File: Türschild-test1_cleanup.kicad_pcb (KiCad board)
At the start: 2 copper layers, 90.2 x 76.2 mm, 84 parts, among them J1 Conn_01x03_Male, J3 USB_B_Micro, J4 Conn_01x24_MountingPin, Q3 Si1442DH, U1 BQ25570, U2 BQ27441-G1, U3 ESP32-WROOM-32, U4 CP2102N-A01-GQFN28

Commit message: HowTo Changes mit Daniel
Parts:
- removed Q3: Si1442DH, Package_TO_SOT_SMD:SOT-363_SC-70-6
- added BT1: 3,7V, Battery:BatteryHolder_Bulgin_BX0036_1xC, F.Cu at (201.7, 34.9)
- added C12: 1µ, Capacitor_SMD:C_0603_1608Metric_Pad1.05x0.95mm_HandSolder, F.Cu at (277.0, 22.8)
- added C24: 100n, Capacitor_SMD:C_0603_1608Metric_Pad1.05x0.95mm_HandSolder, F.Cu at (266.2, 31.9)
- added C25: 100n, Capacitor_SMD:C_0603_1608Metric_Pad1.05x0.95mm_HandSolder, F.Cu at (247.8, 53.2)
- added C26: 4u7, Capacitor_SMD:C_0805_2012Metric_Pad1.15x1.40mm_HandSolder, F.Cu at (240.9, 55.3)
- added J2: Conn_01x03_Female, Connector_PinSocket_2.00mm:PinSocket_1x03_P2.00mm_Vertical_SMD_Pin1Right, F.Cu at (224.9, 56.2)
- added Q1: IRLML2502PbF, Package_TO_SOT_SMD:SOT-23, F.Cu at (261.4, 35.8)
- added R21: 0R, Resistor_SMD:R_0603_1608Metric_Pad1.05x0.95mm_HandSolder, F.Cu at (244.9, 60.7)
- added R22: 1K, Resistor_SMD:R_0603_1608Metric_Pad1.05x0.95mm_HandSolder, F.Cu at (264.7, 40.8)
- added R23: 4K7, Resistor_SMD:R_0603_1608Metric_Pad1.05x0.95mm_HandSolder, F.Cu at (123.2, 121.0)
- added SC1: Solar_Cells, Connector_PinHeader_2.54mm:PinHeader_1x02_P2.54mm_Horizontal, F.Cu at (201.2, 54.2)
- added U5: LM1117-3.3, Package_TO_SOT_SMD:SOT-223-3_TabPin2, F.Cu at (264.1, 25.5)
- added U6: WE-TVS-82400152, Package_TO_SOT_SMD:SOT-563, F.Cu at (119.8, 115.7)
- C1, C10, C11, C2: footprint Capacitor_SMD:C_0603_1608Metric -> Capacitor_SMD:C_0805_2012Metric_Pad1.15x1.40mm_HandSolder
- C13, C14, C15, C16, C17, C18, C19, C20, C21, C22, C5, C6, C7, C8, C9: footprint Capacitor_SMD:C_0603_1608Metric -> Capacitor_SMD:C_0603_1608Metric_Pad1.05x0.95mm_HandSolder
- C3, C4: value 0,1µF -> 100n; footprint Capacitor_SMD:C_0603_1608Metric -> Capacitor_SMD:C_0603_1608Metric_Pad1.05x0.95mm_HandSolder
- D1, D2, D3, D4: footprint LED_SMD:LED_0603_1608Metric_Castellated -> LED_SMD:LED_0603_1608Metric_Pad1.05x0.95mm_HandSolder
- D10, D11, D12: value MBR0530 -> MBR0530T1G
- D5, D6: value D_Schottky_Small -> SS16; footprint Diode_SMD:D_0603_1608Metric_Castellated -> Diode_SMD:D_SMA-SMB_Universal_Handsoldering
- D7, D8, D9: footprint Diode_SMD:D_0603_1608Metric_Castellated -> Diode_SMD:D_0603_1608Metric_Pad1.05x0.95mm_HandSolder
- J1: footprint Connector_Molex:Molex_Micro-Latch_53253-0370_1x03_P2.00mm_Vertical -> Connector_PinHeader_2.00mm:PinHeader_1x03_P2.00mm_Vertical_SMD_Pin1Left
- J3: footprint Connector_USB:USB_Micro-B_Wuerth_614105150721_Vertical_CircularHoles -> Connector_USB:USB_Mini-B_Wuerth_65100516121_Horizontal
- J4: footprint Connector_FFC-FPC:Hirose_FH12-24S-0.5SH_1x24-1MP_P0.50mm_Horizontal -> Connector_FFC-FPC:Molex_502244-2430_1x24-1MP_P0.5mm_Horizontal
- L1, L2, L3: footprint Inductor_SMD:L_0603_1608Metric -> Inductor_SMD:L_Wuerth_WE-TPC-3816
- R1, R10, R11, R12, R13, R14, R15, R16, R17, R18, R19, R2, R20, R24, R26, R3, R4, R5, R6, R7, R8, R9, Rok1, Rok2, Rok3, Rout1, Rout2, Rov1, Rov2: footprint Resistor_SMD:R_0603_1608Metric -> Resistor_SMD:R_0603_1608Metric_Pad1.05x0.95mm_HandSolder
- moved J1 172.0 mm to (272.5, 20.9)
- moved R1 170.2 mm to (273.3, 32.2), turned to 0 degrees
- moved Rov2 169.9 mm to (276.9, 29.7), turned to 0 degrees
- moved C2 162.9 mm to (266.4, 30.1), turned to 0 degrees
- moved D7 159.3 mm to (277.1, 19.7)
- moved Rov1 157.6 mm to (271.5, 35.3), turned to 0 degrees
- moved Rok2 155.9 mm to (271.5, 33.8)
- moved Rok1 153.2 mm to (261.3, 38.3), turned to 0 degrees
- moved L1 146.4 mm to (262.1, 31.6), turned to 0 degrees
- moved C6 144.4 mm to (269.9, 30.8)
- moved Rout1 143.5 mm to (268.1, 38.4), turned to 0 degrees
- moved D5 142.2 mm to (264.6, 19.6), turned to 0 degrees
- moved Rok3 141.5 mm to (251.2, 54.7), turned to 0 degrees
- moved Rout2 139.1 mm to (248.2, 57.7), turned to 0 degrees
- moved R7 137.9 mm to (269.5, 32.3), turned to 0 degrees
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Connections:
- D7 pad 1: Net-(D7-Pad1) -> VBUS
- J3 pad 1: Net-(D7-Pad1) -> VBUS
- J3 pad 2: Net-(D9-Pad1) -> Net-(J3-Pad2)
- J3 pad 3: Net-(D8-Pad1) -> Net-(J3-Pad3)
- J3 pad 6: Net-(J3-Pad6) -> GND
- R20 pad 1: Net-(R20-Pad1) -> GND
- R20 pad 2: GND -> Net-(R20-Pad2)
- R6 pad 1: Net-(R20-Pad1) -> Net-(R20-Pad2)
- R6 pad 2: Net-(D7-Pad1) -> VBUS
- U3 pad 27: Net-(U3-Pad27) -> USBID
- U3 pad 39: (no net) -> GND
- U4 pad 4: Net-(D8-Pad1) -> Net-(U4-Pad4)
- U4 pad 5: Net-(D9-Pad1) -> Net-(U4-Pad5)
- U4 pad 8: Net-(R20-Pad1) -> Net-(R20-Pad2)
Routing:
- net GND: track 476.0 -> 1.35 mm, vias 4 -> 1
- net +3V3: track 161.7 -> 0.00 mm, vias 2 -> 0
- net ESP_EN: track 81.2 -> 0.00 mm, vias 2 -> 0
- net Net-(D8-Pad1): track 69.2 -> 0.00 mm, vias 3 -> 0
- net Net-(D7-Pad1): track 67.1 -> 0.00 mm, vias 1 -> 0
- net Net-(D9-Pad1): track 66.9 -> 0.00 mm, vias 3 -> 0
- net SDA: track 66.5 -> 0.00 mm, vias 4 -> 0
- net ESP_CON_RX: track 65.7 -> 0.00 mm, vias 2 -> 0
- net ESP_CON_TX: track 65.0 -> 0.00 mm, vias 2 -> 0
- net ESP_MOSI: track 64.8 -> 0.00 mm, vias 2 -> 0
- net SCL: track 62.5 -> 0.00 mm, vias 4 -> 0
- net ESP_MISO: track 61.7 -> 0.00 mm, vias 2 -> 0
- net ESP_CS: track 59.5 -> 0.00 mm, vias 2 -> 0
- net VBAT_OK: track 58.2 -> 0.00 mm, vias 2 -> 0
- net ESP_SCK: track 57.1 -> 0.00 mm, vias 2 -> 0
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- added copper zone on B.Cu, net GND
- added copper zone on F.Cu, net GND
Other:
- outline, holes or cut-outs redrawn
- net class Default: clearance 0.2 -> 0.15; trace_width 0.25 -> 0.15
- rule trace_clearance: 0.2 -> 0.15
- rule trace_min: 0.2 -> 0.15

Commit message: Version 1
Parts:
- removed BT1: 3,7V, Battery:BatteryHolder_Bulgin_BX0036_1xC
- removed D8, D9: D_Schottky_Small, Diode_SMD:D_0603_1608Metric_Pad1.05x0.95mm_HandSolder
- removed J2: Conn_01x03_Female, Connector_PinSocket_2.00mm:PinSocket_1x03_P2.00mm_Vertical_SMD_Pin1Right
- moved C12 166.4 mm to (147.3, 127.0)
- moved D7 165.1 mm to (122.6, 77.9), turned to 90 degrees
- moved J1 164.4 mm to (118.1, 77.5), turned to 90 degrees
- moved C6 162.7 mm to (110.5, 63.1), turned to 90 degrees
- moved R22 161.7 mm to (126.0, 124.0)
- moved C7 155.4 mm to (113.9, 73.7), turned to 180 degrees
- moved R3 154.3 mm to (122.9, 64.1), turned to 90 degrees
- moved R7 153.2 mm to (119.4, 62.6), turned to 270 degrees
- moved C9 152.4 mm to (125.8, 65.0), turned to 180 degrees
- moved U5 150.4 mm to (148.6, 121.9)
- moved C24 149.0 mm to (151.5, 127.0), turned to 180 degrees
- moved D5 148.1 mm to (128.3, 77.5), turned to 180 degrees
- moved R1 144.6 mm to (135.5, 76.2), turned to 180 degrees
- moved R26 143.6 mm to (165.1, 116.8), turned to 90 degrees
- moved C25 142.0 mm to (126.0, 126.0)
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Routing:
- net +3V3: track 0.00 -> 203.9 mm, vias 0 -> 4
- net USBID: track 0.00 -> 99.7 mm, vias 0 -> 4
- net Net-(C7-Pad1): track 0.00 -> 98.2 mm, vias 0 -> 4
- net ESP_CON_TX: track 0.00 -> 96.0 mm, vias 0 -> 2
- net ESP_CON_RX: track 0.00 -> 94.6 mm, vias 0 -> 2
- net SCL: track 0.00 -> 93.0 mm, vias 0 -> 4
- net VCC: track 0.00 -> 89.1 mm, vias 0 -> 2
- net SDA: track 0.00 -> 86.9 mm, vias 0 -> 4
- net PREVGL: track 0.00 -> 77.3 mm, vias 0 -> 2
- net GPOUT: track 0.00 -> 71.2 mm, vias 0 -> 5
- net ESP_MOSI: track 0.00 -> 63.4 mm
- net VBUS: track 14.9 -> 74.2 mm
- net ESP_MISO: track 0.00 -> 56.8 mm, vias 0 -> 2
- net ESP_SCK: track 0.00 -> 56.6 mm
- net PREVGH: track 0.00 -> 55.0 mm, vias 0 -> 2
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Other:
- board text added: "n.b"

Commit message: layout verbessert
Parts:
- removed D7: D_Schottky_Small, Diode_SMD:D_0603_1608Metric_Pad1.05x0.95mm_HandSolder
- moved C6 40.8 mm to (151.1, 59.4), turned to 180 degrees
- moved U2 32.4 mm to (146.7, 61.0), turned to 180 degrees
- moved C7 31.7 mm to (142.3, 59.5)
- moved SC1 28.8 mm to (116.0, 53.5)
- moved R3 28.3 mm to (151.1, 60.9), turned to 180 degrees
- moved R7 23.4 mm to (142.3, 57.9), turned to 0 degrees
- moved R4 22.1 mm to (151.1, 62.5), turned to 180 degrees
- moved R19 22.1 mm to (142.3, 61.1), turned to 180 degrees
- moved R5 21.7 mm to (142.3, 62.6), turned to 0 degrees
- moved C9 16.5 mm to (142.3, 64.1), turned to 0 degrees
- moved C8 16.4 mm to (142.3, 65.7), turned to 0 degrees
- moved C15 8.51 mm to (177.0, 102.8), turned to 0 degrees
- moved C18 7.89 mm to (186.4, 108.3)
- moved R1 7.43 mm to (142.9, 75.3), turned to 90 degrees
- moved C22 7.39 mm to (192.5, 108.3)
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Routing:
- net SCL: track 93.0 -> 42.5 mm, vias 4 -> 2
- net GND: track 16.8 -> 64.8 mm, vias 1 -> 11
- net SDA: track 86.9 -> 43.1 mm, vias 4 -> 2
- net PREVGL: track 77.3 -> 41.3 mm
- net GPOUT: track 71.2 -> 38.0 mm, vias 5 -> 2
- net Net-(R7-Pad2): track 41.4 -> 18.2 mm, vias 0 -> 2
- net +3V3: track 203.9 -> 181.0 mm, vias 4 -> 2
- net Net-(C7-Pad1): track 98.2 -> 118.2 mm, vias 4 -> 2
- net Net-(C2-Pad1): track 15.8 -> 2.80 mm
- net Net-(Rout1-Pad2): track 14.5 -> 5.17 mm
- net Net-(D6-Pad2): track 30.1 -> 21.5 mm, vias 2 -> 0
- net Net-(C1-Pad1): track 26.2 -> 17.8 mm
- net Net-(C18-Pad2): track 11.5 -> 3.10 mm
- net Net-(C3-Pad1): track 28.1 -> 19.8 mm
- net Net-(C22-Pad2): track 14.5 -> 7.90 mm
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
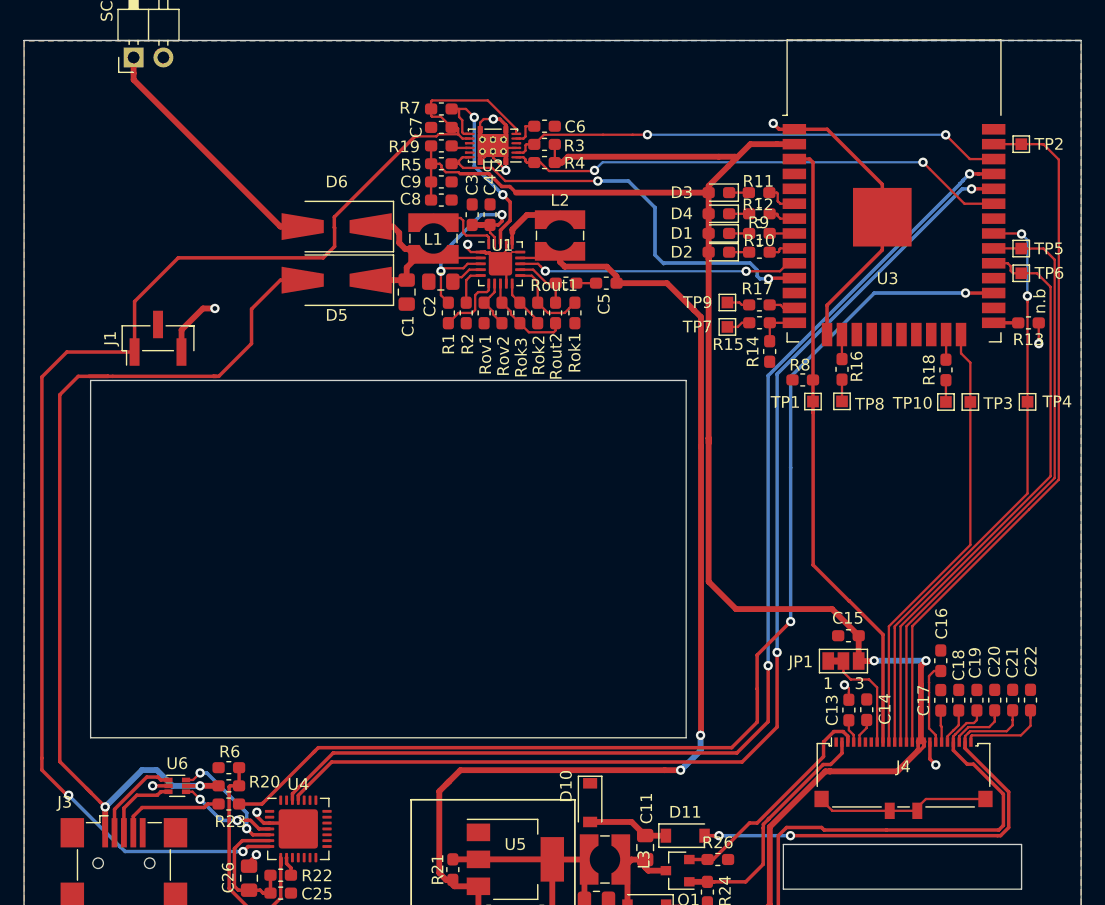
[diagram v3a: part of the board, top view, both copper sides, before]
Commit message: Akkustecker hinzugefügt layout verbessert
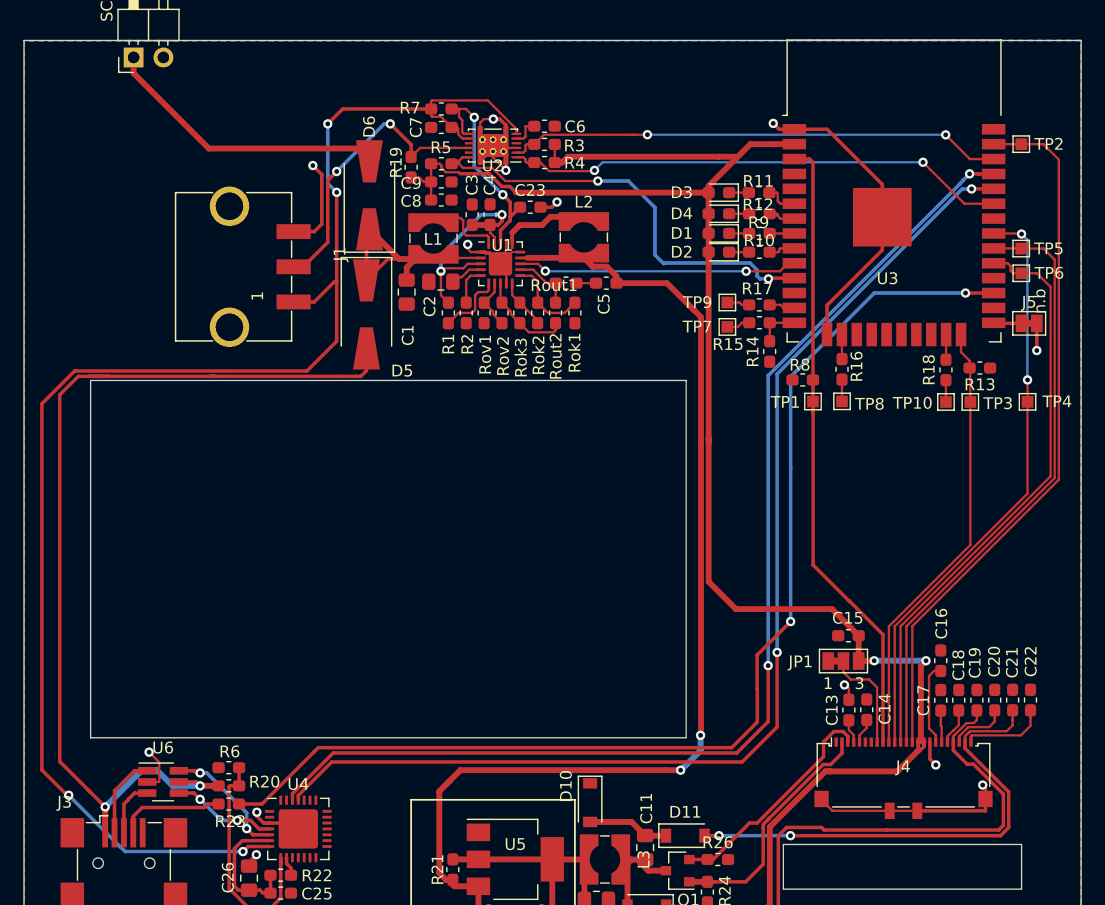
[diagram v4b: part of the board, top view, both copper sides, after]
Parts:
- added C23: 100n, Capacitor_SMD:C_0603_1608Metric_Pad1.05x0.95mm_HandSolder, F.Cu at (149.9, 66.3)
- added J5: PROG, Jumper:SolderJumper-2_P1.3mm_Bridged_Pad1.0x1.5mm, F.Cu at (192.4, 76.2)
- J1: value Conn_01x03_Male -> 662103130822smt; footprint Connector_PinHeader_2.00mm:PinHeader_1x03_P2.00mm_Vertical_SMD_Pin1Left -> Tuerschild-Kiacad:662103130822
- R13: value n.b -> 4K7
- U6: value WE-TVS-82400152 -> WE-TVS-82400102; footprint Package_TO_SOT_SMD:SOT-563 -> Package_TO_SOT_SMD:SOT-23-6_Handsoldering
- moved J1 8.62 mm to (124.2, 71.4), turned to 270 degrees
- moved R13 5.66 mm to (188.2, 80.0)
- moved D5 3.87 mm to (135.9, 75.4), turned to 270 degrees
- moved D6 3.86 mm to (136.1, 65.3), turned to 90 degrees
- moved R19 3.16 mm to (139.7, 62.9), turned to 270 degrees
- moved L2 2.04 mm to (154.4, 68.9)
- moved U6 1.26 mm to (118.5, 115.3)
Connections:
- J4 pad MP: Net-(J4-PadMP) -> GND
- R13 pad 2: Net-(R13-Pad2) -> ESP_HS
- R19 pad 1: Net-(R19-Pad1) -> BIN
- U2 pad 10: Net-(R19-Pad1) -> BIN
- U3 pad 25: Net-(R13-Pad2) -> Net-(J5-Pad1)
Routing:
- net BIN: track 0.00 -> 25.5 mm, vias 0 -> 2
- net GND: track 64.8 -> 87.8 mm, vias 11 -> 13
- net Net-(J4-PadMP): track 15.0 -> 0.00 mm
- net Net-(C7-Pad1): track 118.2 -> 127.7 mm, vias 2 -> 4
- net Net-(C1-Pad1): track 17.8 -> 23.7 mm
- net VBUS: track 80.6 -> 83.9 mm
- net Net-(D6-Pad2): track 21.5 -> 24.6 mm
- net Net-(J5-Pad1): track 0.00 -> 2.40 mm
- net Net-(R13-Pad2): track 2.10 -> 0.00 mm
- net Net-(L2-Pad1): track 5.84 -> 7.68 mm
- net Net-(J3-Pad3): track 6.48 -> 4.84 mm
- net Net-(R19-Pad1): track 1.63 -> 0.00 mm
- net Net-(C23-Pad1): track 18.2 -> 19.3 mm
- net Net-(J3-Pad2): track 7.84 -> 7.07 mm
- net Net-(U4-Pad4): track 8.45 -> 9.01 mm

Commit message: Update 22.10.20
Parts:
- added ?: , , F.Cu at (192.8, 89.4)
- added ?: , , F.Cu at (193.0, 97.3)
- added ?: , , F.Cu at (193.0, 87.9)
- added J6: Conn_01x08_Female, Connector_PinHeader_1.00mm:PinHeader_1x08_P1.00mm_Vertical_SMD_Pin1Left, F.Cu at (193.3, 93.2)
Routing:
- net ESP_EN: track 54.2 -> 72.8 mm, vias 0 -> 2
- net +3V3: track 181.3 -> 196.7 mm
- net ESP_HS: track 38.0 -> 46.6 mm
- net ESP_MISO: track 50.6 -> 56.0 mm, vias 2 -> 4
- net ESP_MOSI: track 61.0 -> 65.5 mm
- net ESP_SCK: track 52.0 -> 56.3 mm
- net ESP_CS: track 50.1 -> 53.8 mm
- net Net-(C1-Pad1): track 23.7 -> 24.9 mm
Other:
- board text added: "3V3"
- board text added: "BUSY"
- board text added: "CLK"
- board text added: "CS"
- board text added: "DC"
- board text added: "DIN"
- board text added: "GND"
- board text added: "RST"

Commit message: Plotten
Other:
- board text added: "Dommel GmbH"
- board text added: "M.Mardini"
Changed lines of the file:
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@@
   (general
     (thickness 1.6)
-    (drawings 26)
+    (drawings 28)
     (tracks 886)
     (zones 0)
@@
     (32 B.Adhes user hide)
     (33 F.Adhes user hide)
-    (34 B.Paste user hide)
+    (34 B.Paste user)
     (35 F.Paste user)
     (36 B.SilkS user hide)
@@
   )
   (setup
-    (last_trace_width 0.5)
+    (last_trace_width 0.15)
     (user_trace_width 0.15)
     (user_trace_width 0.2)
@@
       (outputformat 1)
       (mirror false)
-      (drillshape 1)
+      (drillshape 0)
       (scaleselection 1)
-      (outputdirectory ""))
+      (outputdirectory "bestellen/"))
   )
   (net 0 "")
@@
     (tags "solder jumper open")
     (attr virtual)
-    (fp_text reference J5 (at 0 -1.8) (layer F.SilkS)
+    (fp_text reference J5 (at 0.112 2.286) (layer F.SilkS)
       (effects (font (size 1 1) (thickness 0.15)))
     )
@@
     (tags "resistor handsolder")
     (attr smd)
-    (fp_text reference Rout1 (at 1.016 -0.2032 180) (layer F.SilkS)
+    (fp_text reference Rout1 (at 0.127 1.397 180) (layer F.SilkS)
       (effects (font (size 1 1) (thickness 0.15)))
     )
@@
     (tags "Mini USB 2.0 Type B")
     (attr smd)
-    (fp_text reference J3 (at -5.05 -5.2) (layer F.SilkS)
+    (fp_text reference J3 (at -0.392 -5.029) (layer F.SilkS)
       (effects (font (size 1 1) (thickness 0.15)))
     )
@@
     (tags "capacitor handsolder")
     (attr smd)
-    (fp_text reference C7 (at 2.145 0 90) (layer F.SilkS)
+    (fp_text reference C7 (at 2.5794 -0.2032 180) (layer F.SilkS)
       (effects (font (size 1 1) (thickness 0.15)))
     )
@@
     (tags "solder jumper open")
     (attr virtual)
-    (fp_text reference JP1 (at -3.63776 0.06604) (layer F.SilkS)
+    (fp_text reference JP1 (at -3.6022 0.0254) (layer F.SilkS)
       (effects (font (size 1 1) (thickness 0.15)))
     )
@@
     (tags "wurth wuerth smd inductor")
     (attr smd)
-    (fp_text reference L3 (at 0 3.33 90) (layer F.SilkS)
+    (fp_text reference L3 (at 3.4417 0.8662 90) (layer F.SilkS)
       (effects (font (size 1 1) (thickness 0.15)))
     )
@@
     (tags "resistor handsolder")
     (attr smd)
-    (fp_text reference R6 (at -0.075 2.9 180) (layer F.SilkS)
+    (fp_text reference R6 (at -2.723 -0.047 180) (layer F.SilkS)
       (effects (font (size 1 1) (thickness 0.15)))
     )
@@
     (tags "resistor handsolder")
     (attr smd)
-    (fp_text reference R9 (at 0.0648 0.9144) (layer F.SilkS)
+    (fp_text reference R9 (at 0.1156 -0.8128) (layer F.SilkS)
       (effects (font (size 1 1) (thickness 0.15)))
     )
@@
     (tags "resistor handsolder")
     (attr smd)
-    (fp_text reference R10 (at 0.014 0.9906) (layer F.SilkS)
+    (fp_text reference R10 (at -0.0114 -1.3716) (layer F.SilkS)
       (effects (font (size 1 1) (thickness 0.15)))
     )
@@
     (tags "resistor handsolder")
     (attr smd)
-    (fp_text reference R11 (at 0.0648 0.9652) (layer F.SilkS)
+    (fp_text reference R11 (at -0.0368 1.4224) (layer F.SilkS)
       (effects (font (size 1 1) (thickness 0.15)))
     )
@@
     (tags "resistor handsolder")
     (attr smd)
-    (fp_text reference R12 (at 0.1156 0.762) (layer F.SilkS)
+    (fp_text reference R12 (at 0.1156 0.9398) (layer F.SilkS)
       (effects (font (size 1 1) (thickness 0.15)))
     )
@@
     (tags "resistor handsolder")
     (attr smd)
-    (fp_text reference R14 (at 0.0254 1.4224 90) (layer F.SilkS)
+    (fp_text reference R14 (at 3.316 -0.0254 90) (layer F.SilkS)
       (effects (font (size 1 1) (thickness 0.15)))
     )
@@
     (tags "resistor handsolder")
     (attr smd)
-    (fp_text reference R15 (at -2.6784 1.8542) (layer F.SilkS)
+    (fp_text reference R15 (at -0.635 2.2098 90) (layer F.SilkS)
       (effects (font (size 1 1) (thickness 0.15)))
     )
@@
     (tags "resistor handsolder")
     (attr smd)
-    (fp_text reference R20 (at 3.05 1.225 180) (layer F.SilkS)
+    (fp_text reference R20 (at 3.104 -0.054 180) (layer F.SilkS)
       (effects (font (size 1 1) (thickness 0.15)))
     )
@@
     (tags "resistor handsolder")
     (attr smd)
-    (fp_text reference R26 (at 0 -1.43) (layer F.SilkS)
+    (fp_text reference R26 (at 1.1443 -1.43) (layer F.SilkS)
       (effects (font (size 1 1) (thickness 0.15)))
     )
@@
     (descr "Through hole angled pin header, 1x02, 2.54mm pitch, 6mm pin length, single row")
     (tags "Through hole angled pin header THT 1x02 2.54mm single row")
-    (fp_text reference SC1 (at 4.385 -2.27 90) (layer F.SilkS)
+    (fp_text reference SC1 (at -0.7112 5.3848 90) (layer F.SilkS)
       (effects (font (size 1 1) (thickness 0.15)))
     )
@@
     (tags "test point SMD pad rectangle square")
     (attr virtual)
-    (fp_text reference TP1 (at 2.34442 -0.07366) (layer F.SilkS)
+    (fp_text reference TP1 (at 0.1143 -1.9685) (layer F.SilkS)
       (effects (font (size 1 1) (thickness 0.15)))
     )
@@
     (tags "QFN NoLead")
     (attr smd)
-    (fp_text reference U1 (at 0.1524 -1.5748) (layer F.SilkS)
+    (fp_text reference U1 (at 0.889 -3.048) (layer F.SilkS)
       (effects (font (size 1 1) (thickness 0.15)))
     )
@@
     (tags "SON thermal pads")
     (attr smd)
-    (fp_text reference U2 (at 0.0254 -1.7272) (layer F.SilkS)
+    (fp_text reference U2 (at 0.0254 2.8702) (layer F.SilkS)
       (effects (font (size 1 1) (thickness 0.15)))
     )
@@
     )
   )
+  (gr_text M.Mardini (at 194.183 127.127) (layer F.SilkS)
+    (effects (font (size 0.5 0.5) (thickness 0.1)))
+  )
+  (gr_text "Dommel GmbH\n" (at 187.96 125.73) (layer F.SilkS)
+    (effects (font (size 1.5 1.5) (thickness 0.3)))
+  )
   (gr_text "CLK\n" (at 190.246 93.726) (layer F.SilkS)
     (effects (font (size 0.5 0.5) (thickness 0.125)))
@@
     (effects (font (size 0.5 0.5) (thickness 0.125)))
   )
-  (gr_text n.b (at 193.32956 74.31532 90) (layer F.SilkS)
+  (gr_text n.b (at 194.818 76.073 90) (layer F.SilkS)
     (effects (font (size 1 1) (thickness 0.25)))
   )
